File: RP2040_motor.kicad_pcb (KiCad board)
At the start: 4 copper layers, 85.5 x 54 mm, 162 parts, among them J1 USB_C_Receptacle_USB2.0, J2 Conn_01x05, J3 Conn_01x06, J4 Conn_01x04, J5 Conn_01x04, J6 Conn_01x03, SW1 SW_MEC_5G, U1 EG2131, U10 EG2131, U11 RP2040, U2 EG2131, U3 LM358, U4 EG2131, U5 EG2131, U6 XL7045, U7 NCP1117-3.3_SOT223, U8 EG2131, U9 W25Q128JVS, Y1 Crystal_GND24

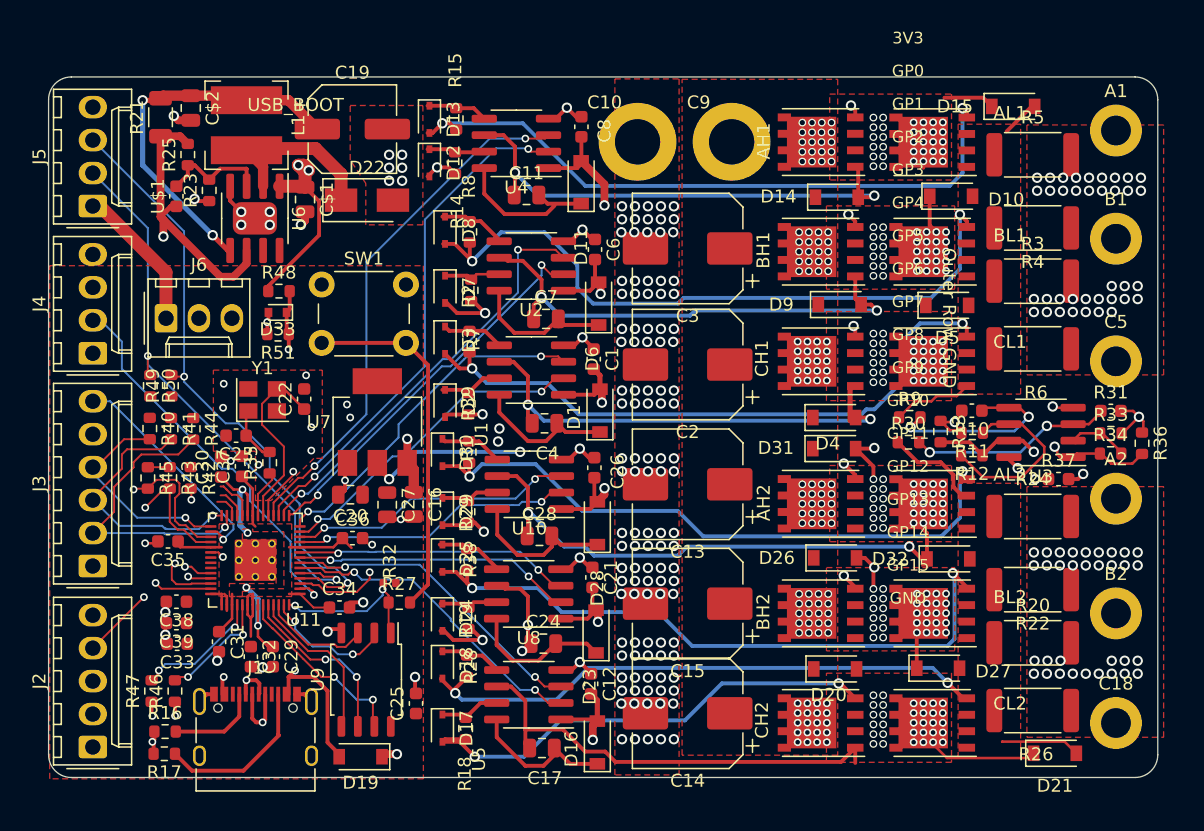
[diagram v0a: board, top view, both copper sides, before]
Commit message: Update files for price quote. DO NOT ORDER THESE BOARDS FROM THIS COMMIT!
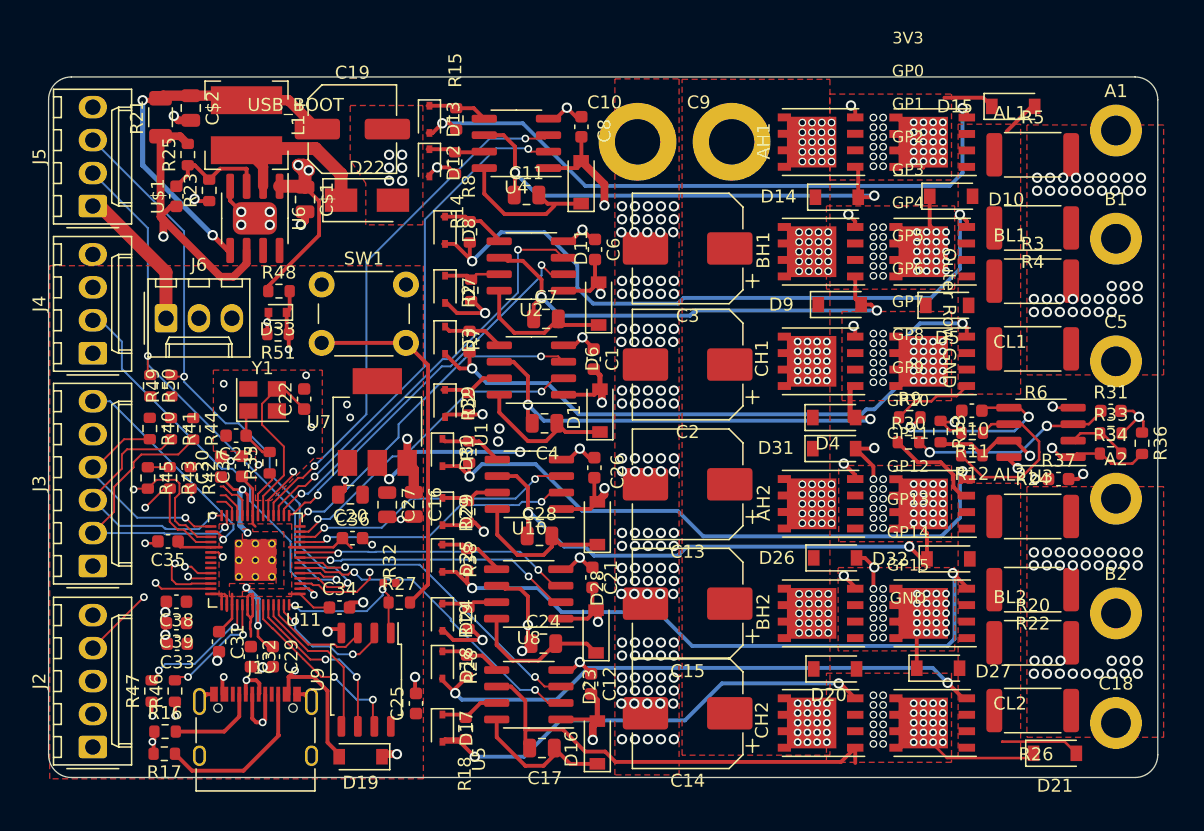
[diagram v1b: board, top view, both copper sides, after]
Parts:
- R51: value 5k -> 5.1k

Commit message: In progress independent phase current measurement.
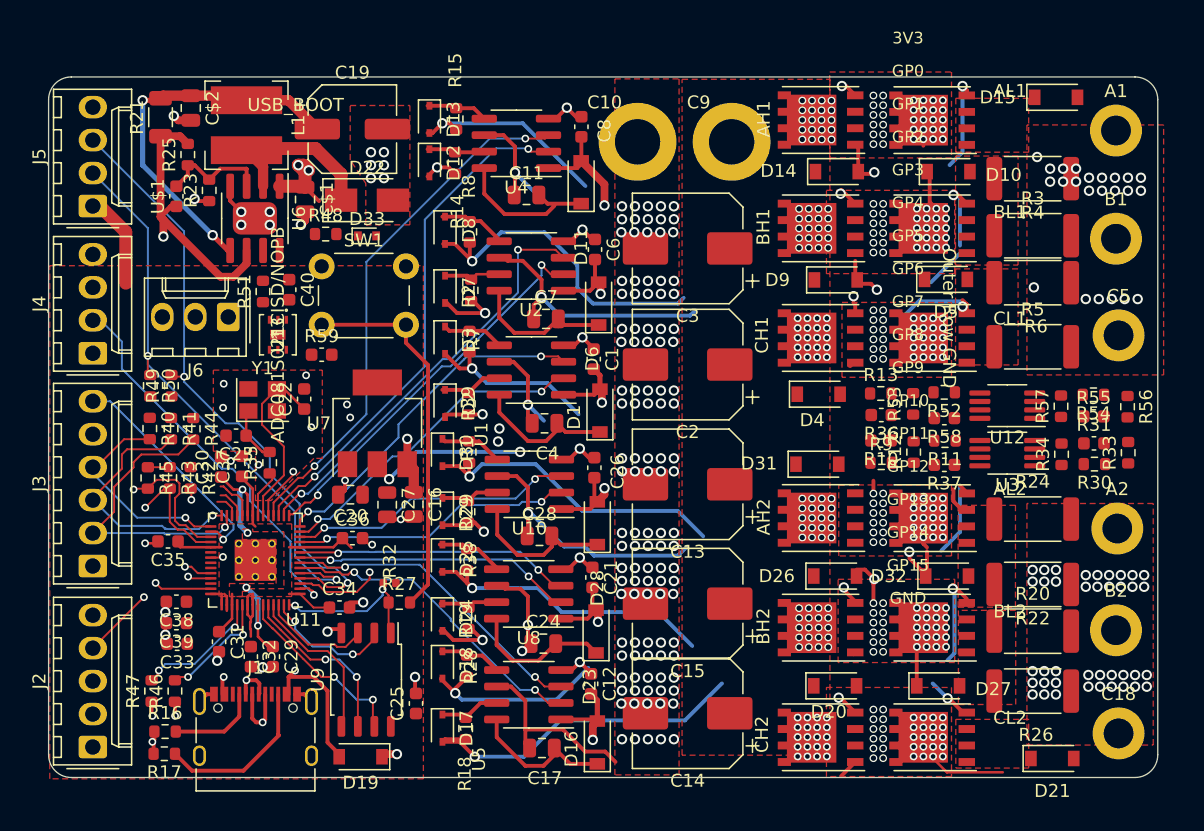
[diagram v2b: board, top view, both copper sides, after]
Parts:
- added C40: 1u, Capacitor_SMD:C_0603_1608Metric, F.Cu at (92.9, 84.4)
- added R52: 4.64k, Resistor_SMD:R_0603_1608Metric, F.Cu at (143.4, 92.3)
- added R53: 133k, Resistor_SMD:R_0603_1608Metric, F.Cu at (141.0, 93.2)
- added R54: 499R, Resistor_SMD:R_0603_1608Metric, F.Cu at (154.9, 92.5)
- added R55: 0.1uF, Capacitor_SMD:C_0603_1608Metric, F.Cu at (154.9, 94.2)
- added R56: 4.64k, Resistor_SMD:R_0603_1608Metric, F.Cu at (157.5, 93.4)
- added R57: 133k, Resistor_SMD:R_0603_1608Metric, F.Cu at (152.4, 93.4)
- added R58: 0.1uF, Capacitor_SMD:C_0603_1608Metric, F.Cu at (143.4, 94.3)
- added R59: 0.1uF, Capacitor_SMD:C_0603_1608Metric, F.Cu at (95.4, 89.4)
- added U12: LM358, Package_SO:MSOP-8_3x3mm_P0.65mm, F.Cu at (148.2, 93.3)
- added U13: ADC081S021CISD/NOPB, ADC081S021:ADC081S021CISD&slash_NOPB, F.Cu at (92.0, 87.9)
- R11, R33: value 6.04k -> 4.64k
- R12, R34: value 88.7K -> 133k
- R13: value DNS -> 499R
- R20, R22, R24, R26, R3, R4, R5, R6: value 8mΩ -> 4mΩ
- R30, R9: value 1.1k -> 499R
- R36: value DNS -> 0.1uF; footprint Resistor_SMD:R_0603_1608Metric -> Capacitor_SMD:C_0603_1608Metric
- U3: footprint Package_SO:SOIC-8_3.9x4.9mm_P1.27mm -> Package_SO:MSOP-8_3x3mm_P0.65mm
- moved R36 20.2 mm to (138.5, 94.1), turned to 180 degrees
- moved R5 14.8 mm to (150.2, 88.8)
- moved R30 14.4 mm to (155.0, 97.8), turned to 180 degrees
- moved D33 9.08 mm to (98.9, 80.2), turned to 0 degrees
- moved R37 8.87 mm to (143.4, 97.9), turned to 180 degrees
- moved R10 7.37 mm to (138.5, 96.0)
- moved R48 5.69 mm to (95.7, 80.1)
- moved R13 5.46 mm to (138.5, 92.4), turned to 0 degrees
- moved R6 5.10 mm to (150.2, 83.9)
- moved J6 4.80 mm to (88.2, 86.5), turned to 180 degrees
- moved R12 4.49 mm to (141.0, 96.9), turned to 90 degrees
- moved R9 4.13 mm to (138.5, 97.7)
- moved R4 3.80 mm to (150.2, 75.8)
- moved R34 3.78 mm to (152.4, 97.1), turned to 90 degrees
- moved R3 3.50 mm to (150.2, 80.2)
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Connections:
- AL1 pad 1: VSENSE2 -> GND
- AL2 pad 1: VSENSE1 -> VSENSE1A
- BL1 pad 1: VSENSE2 -> VSENSE2B
- BL2 pad 1: VSENSE1 -> VSENSE1B
- CL1 pad 1: VSENSE2 -> VSENSE2C
- CL2 pad 1: VSENSE1 -> GND
- D10 pad 2: VSENSE2 -> VSENSE2B
- D15 pad 2: VSENSE2 -> GND
- D21 pad 2: VSENSE1 -> GND
- D27 pad 2: VSENSE1 -> VSENSE1B
- D32 pad 2: VSENSE1 -> VSENSE1A
- D33 pad 1: A3 -> Net-(U13-Pad3)
- D5 pad 2: VSENSE2 -> VSENSE2C
- J6 pad 1: +3V3 -> /RUN
- J6 pad 2: A4 -> /SWCLK
- J6 pad 3: GND -> /SWD
- R12 pad 1: A2 -> A4
- R12 pad 2: Net-(R11-Pad1) -> Net-(R10-Pad1)
- R13 pad 1: GND -> VSENSE2B
- R13 pad 2: A2 -> Net-(R13-Pad2)
- R20 pad 2: VSENSE1 -> VSENSE1B
- R22 pad 2: VSENSE1 -> VSENSE1A
- R24 pad 2: VSENSE1 -> VSENSE1A
- R26 pad 2: VSENSE1 -> VSENSE1B
- R3 pad 2: VSENSE2 -> VSENSE2B
- R30 pad 1: VSENSE1 -> VSENSE1A
- R34 pad 1: A1 -> A3
- R34 pad 2: Net-(R33-Pad1) -> Net-(R30-Pad2)
- R36 pad 1: GND -> Net-(R13-Pad2)
- R36 pad 2: A1 -> GND
- R4 pad 2: VSENSE2 -> VSENSE2B
- R48 pad 2: A3 -> Net-(U13-Pad3)
- R5 pad 2: VSENSE2 -> VSENSE2C
- R51 pad 1: A3 -> Net-(U13-Pad3)
- R6 pad 2: VSENSE2 -> VSENSE2C
- R9 pad 1: VSENSE2 -> VSENSE1B
- U11 pad 34: ENCC -> ADC_CLK
- U11 pad 35: /GPIO23 -> ENCC
- U11 pad 36: /GPIO24 -> ADC_DATA
- U11 pad 37: /GPIO25 -> ADC_CS
- U3 pad 1: A1 -> A3
- U3 pad 7: A2 -> A4
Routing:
- net A1: track 89.8 -> 37.4 mm, vias 4 -> 3
- net A2: track 86.8 -> 38.7 mm, vias 4 -> 3
- net +3V3: track 95.7 -> 55.3 mm, vias 4 -> 2
- net Net-(CH1-Pad2): track 38.8 -> 4.06 mm
- net A3: track 30.0 -> 0.00 mm, vias 2 -> 0
- net M2A: track 43.2 -> 13.3 mm
- net M2C: track 37.2 -> 8.33 mm, vias 34 -> 33
- net Net-(AL1-Pad2): track 51.1 -> 23.0 mm
- net Net-(CL2-Pad2): track 44.8 -> 18.3 mm
- net Net-(CL1-Pad2): track 49.3 -> 23.0 mm
- net Net-(BH1-Pad2): track 39.5 -> 16.1 mm
- net Net-(AH1-Pad2): track 42.6 -> 21.0 mm
- net M1C: track 45.0 -> 23.9 mm
- net M1A: track 46.7 -> 26.2 mm, vias 35 -> 34
- net Net-(BL2-Pad2): track 50.5 -> 30.8 mm
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- added copper zone on F.Cu, net VSENSE1A
- added copper zone on F.Cu, net VSENSE1B
- added copper zone on F.Cu, net VSENSE2B
- added copper zone on F.Cu, net VSENSE2C
- removed copper zone on F.Cu, net VSENSE1
- removed copper zone on F.Cu, net VSENSE2

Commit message: Break out to two page schematic. Update images and schematic PDF
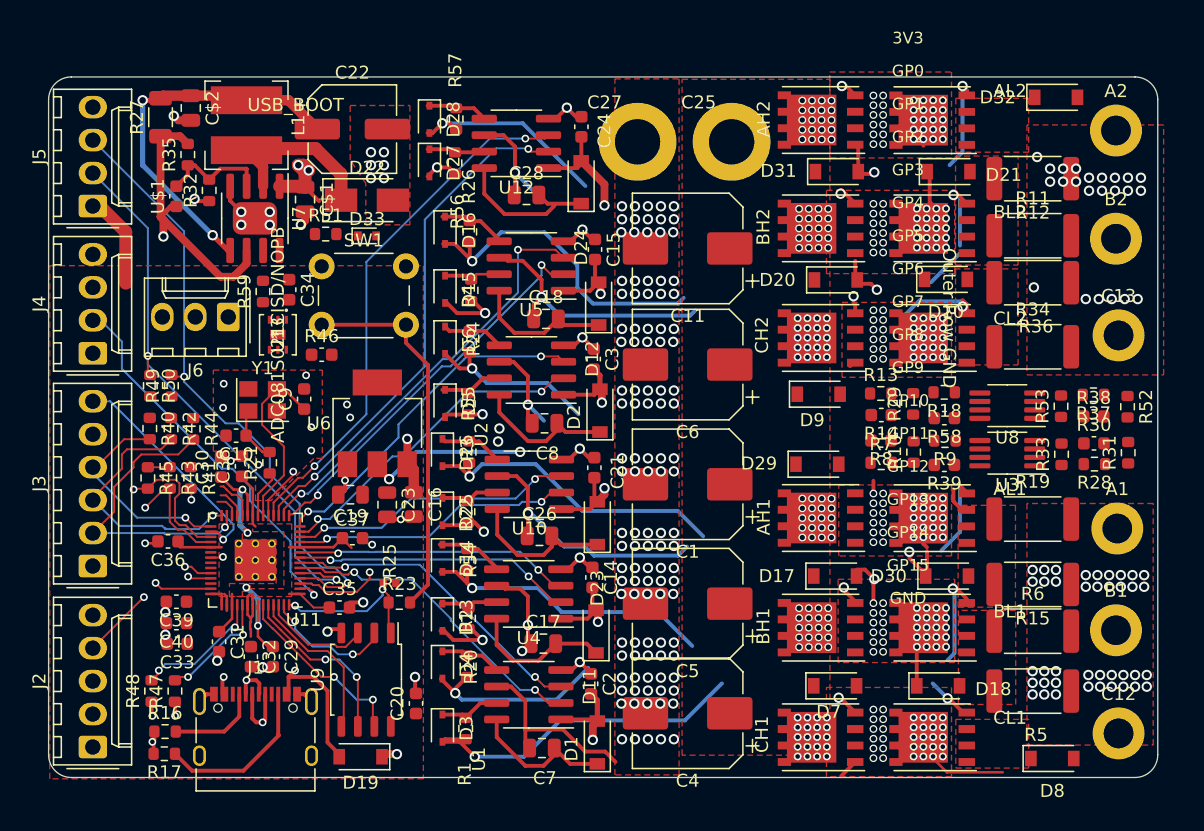
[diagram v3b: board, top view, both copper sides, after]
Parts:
- renumbered A2 to A1, A1 to A2, AH2 to AH1, AH1 to AH2, AL2 to AL1, AL1 to AL2, B2 to B1, B1 to B2, BH2 to BH1, BH1 to BH2, BL2 to BL1, BL1 to BL2, C13 to C1, C23 to C10, C3 to C11, C18 to C12, C5 to C13, C21 to C14, C6 to C15, C24 to C17, C7 to C18, C20 to C19, C12 to C2, C25 to C20, C26 to C21, C19 to C22, C27 to C23, C8 to C24, C9 to C25, C28 to C26, C10 to C27, C11 to C28, C1 to C3, C40 to C34, C34 to C35, C35 to C36, C36 to C37, C37 to C38, C38 to C39, C14 to C4, C39 to C40, C15 to C5, C2 to C6, C17 to C7, C4 to C8, C22 to C9, CH2 to CH1, CH1 to CH2, CL2 to CL1, CL1 to CL2, D16 to D1, D5 to D10, D23 to D11, D6 to D12, D24 to D13, D25 to D14, D7 to D15, D8 to D16, D26 to D17, D27 to D18, D1 to D2, D9 to D20, D10 to D21, D28 to D23, D11 to D24, D29 to D25, D30 to D26, D12 to D27, D13 to D28, D31 to D29, D17 to D3, D32 to D30, D14 to D31, D15 to D32, D18 to D4, D2 to D5, D3 to D6, D20 to D7, D21 to D8, D4 to D9, R18 to R1, R12 to R10, R3 to R11, R4 to R12, R36 to R14, R22 to R15, R52 to R18, R24 to R19, R19 to R2, R28 to R20, R35 to R21, R29 to R22, R27 to R23, R7 to R24, R32 to R25, R8 to R26, R21 to R27, R30 to R28, R53 to R29, R1 to R3, R31 to R30, R33 to R31, R23 to R32, R34 to R33, R5 to R34, R25 to R35, R6 to R36, R54 to R37, R55 to R38, R37 to R39, R2 to R4, R42 to R41, R41 to R42, R59 to R46, R46 to R47, R47 to R48, R26 to R5, R48 to R51, R56 to R52, R57 to R53, R38 to R54, R39 to R55, R14 to R56, R15 to R57, R51 to R59, R20 to R6, R9 to R7, R10 to R8, R11 to R9, U5 to U1, U4 to U12, U1 to U2, U8 to U4, U2 to U5, U7 to U6, U6 to U7, U12 to U8
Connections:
- net /QSPI_SCLK renamed /power_and_cpu/QSPI_SCLK
- net /QSPI_SD0 renamed /power_and_cpu/QSPI_SD0
- net /QSPI_SD1 renamed /power_and_cpu/QSPI_SD1
- net /QSPI_SD2 renamed /power_and_cpu/QSPI_SD2
- net /QSPI_SD3 renamed /power_and_cpu/QSPI_SD3
- net /QSPI_SS renamed /power_and_cpu/QSPI_SS
- net /RUN renamed /power_and_cpu/RUN
- net /SWCLK renamed /power_and_cpu/SWCLK
- net /SWD renamed /power_and_cpu/SWD
- net /USB_D+ renamed /power_and_cpu/USB_D+
- net /USB_D- renamed /power_and_cpu/USB_D-
- net /XIN renamed /power_and_cpu/XIN
- net /XOUT renamed /power_and_cpu/XOUT
- net /~{USB_BOOT} renamed /power_and_cpu/~{USB_BOOT}
- U1 pad 2: /GPIO4 -> /gate_drive/GPIO4
- U1 pad 3: /GPIO5 -> /gate_drive/GPIO5
- U10 pad 2: /GPIO8 -> /gate_drive/GPIO8
- U10 pad 3: /GPIO9 -> /gate_drive/GPIO9
- U11 pad 11: /GPIO8 -> /power_and_cpu/GPIO8
- U11 pad 12: /GPIO9 -> /power_and_cpu/GPIO9
- U11 pad 13: /GPIO10 -> /power_and_cpu/GPIO10
- U11 pad 14: /GPIO11 -> /power_and_cpu/GPIO11
- U11 pad 15: /GPIO12 -> /power_and_cpu/GPIO12
- U11 pad 16: /GPIO13 -> /power_and_cpu/GPIO13
- U11 pad 17: /GPIO14 -> /power_and_cpu/GPIO14
- U11 pad 18: /GPIO15 -> /power_and_cpu/GPIO15
- U11 pad 6: /GPIO4 -> /power_and_cpu/GPIO4
- U11 pad 7: /GPIO5 -> /power_and_cpu/GPIO5
- U11 pad 8: /GPIO6 -> /power_and_cpu/GPIO6
- U11 pad 9: /GPIO7 -> /power_and_cpu/GPIO7
- U12 pad 2: /GPIO14 -> /gate_drive/GPIO14
- U12 pad 3: /GPIO15 -> /gate_drive/GPIO15
- U2 pad 2: /GPIO10 -> /gate_drive/GPIO10
- U2 pad 3: /GPIO11 -> /gate_drive/GPIO11
- U4 pad 2: /GPIO6 -> /gate_drive/GPIO6
- U4 pad 3: /GPIO7 -> /gate_drive/GPIO7
- U5 pad 2: /GPIO12 -> /gate_drive/GPIO12
- U5 pad 3: /GPIO13 -> /gate_drive/GPIO13
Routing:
- net /power_and_cpu/GPIO15: track 0.00 -> 40.8 mm, vias 0 -> 2
- net /GPIO15: track 40.8 -> 0.00 mm, vias 2 -> 0
- net /gate_drive/GPIO14: track 0.00 -> 39.7 mm, vias 0 -> 2
- net /GPIO14: track 39.7 -> 0.00 mm, vias 2 -> 0
- net /power_and_cpu/GPIO13: track 0.00 -> 32.5 mm, vias 0 -> 2
- net /GPIO13: track 32.5 -> 0.00 mm, vias 2 -> 0
- net /power_and_cpu/GPIO12: track 0.00 -> 30.1 mm, vias 0 -> 2
- net /GPIO12: track 30.1 -> 0.00 mm, vias 2 -> 0
- net /gate_drive/GPIO11: track 0.00 -> 26.8 mm, vias 0 -> 2
- net /GPIO11: track 26.8 -> 0.00 mm, vias 2 -> 0
- net /power_and_cpu/GPIO10: track 0.00 -> 25.4 mm, vias 0 -> 2
- net /GPIO10: track 25.4 -> 0.00 mm, vias 2 -> 0
- net /power_and_cpu/GPIO4: track 0.00 -> 24.7 mm, vias 0 -> 2
- net /GPIO4: track 24.7 -> 0.00 mm, vias 2 -> 0
- net /gate_drive/GPIO5: track 0.00 -> 24.2 mm, vias 0 -> 2
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
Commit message: Updated design rules and fixed routing to eliminate all copper DRC errors.
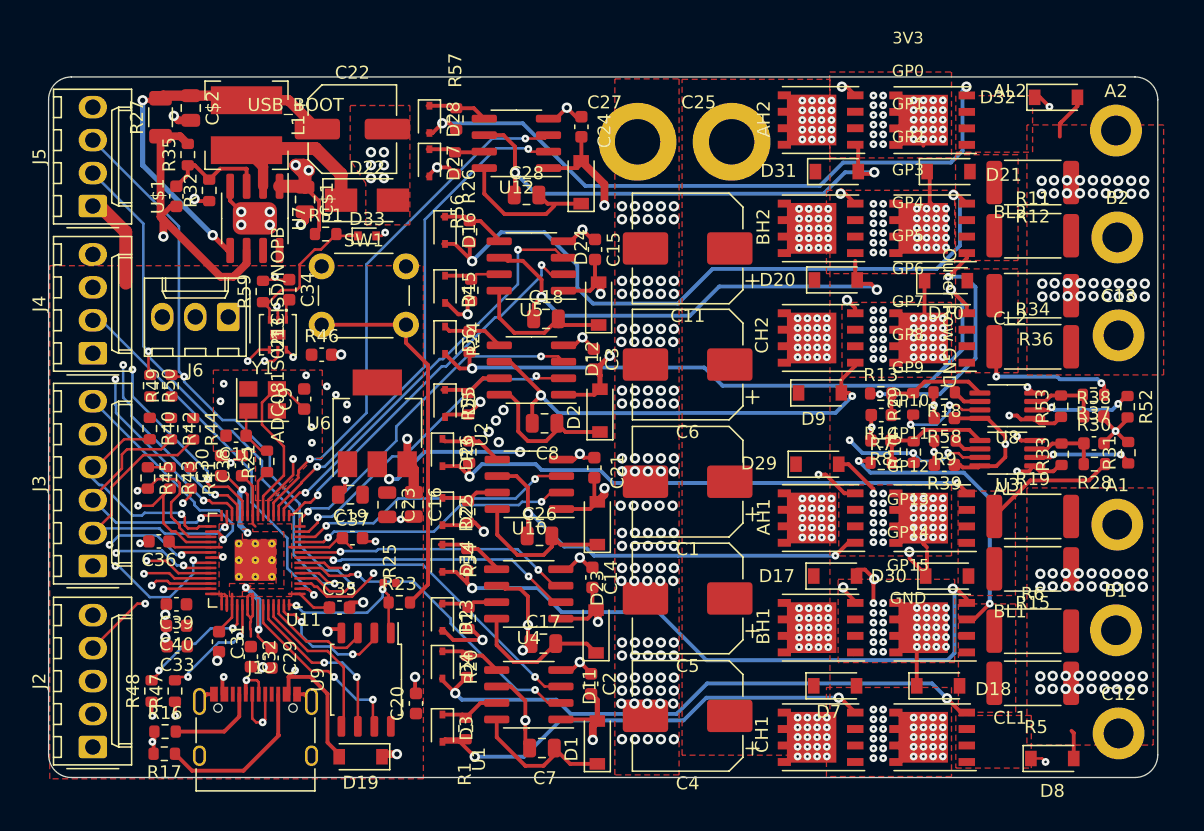
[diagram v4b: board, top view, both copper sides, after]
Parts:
- moved R15 1.20 mm to (150.2, 105.9)
- moved R36 1.00 mm to (150.2, 84.9)
- moved C36 0.70 mm to (82.8, 103.8)
- moved R5 0.60 mm to (150.2, 114.7)
- moved C5 0.40 mm to (123.6, 108.2)
- moved A1 0.30 mm to (156.7, 102.5)
- moved R12 0.30 mm to (150.2, 76.1)
- moved R21 0.22 mm to (91.2, 97.6)
- moved C1 0.20 mm to (123.6, 99.2)
- moved C33 0.20 mm to (84.3, 111.9)
- moved C39 0.20 mm to (84.2, 108.7)
- moved C4 0.20 mm to (123.6, 117.2)
- moved C40 0.20 mm to (84.2, 110.3)
- moved R19 0.20 mm to (150.2, 101.9)
- moved D9 0.14 mm to (133.8, 92.4)
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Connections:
- U1 pad 2: /gate_drive/GPIO4 -> GPIO4
- U1 pad 3: /gate_drive/GPIO5 -> GPIO5
- U10 pad 2: /gate_drive/GPIO8 -> GPIO8
- U10 pad 3: /gate_drive/GPIO9 -> GPIO9
- U11 pad 11: /power_and_cpu/GPIO8 -> GPIO8
- U11 pad 12: /power_and_cpu/GPIO9 -> GPIO9
- U11 pad 13: /power_and_cpu/GPIO10 -> GPIO10
- U11 pad 14: /power_and_cpu/GPIO11 -> GPIO11
- U11 pad 15: /power_and_cpu/GPIO12 -> GPIO12
- U11 pad 16: /power_and_cpu/GPIO13 -> GPIO13
- U11 pad 17: /power_and_cpu/GPIO14 -> GPIO14
- U11 pad 18: /power_and_cpu/GPIO15 -> GPIO15
- U11 pad 6: /power_and_cpu/GPIO4 -> GPIO4
- U11 pad 7: /power_and_cpu/GPIO5 -> GPIO5
- U11 pad 8: /power_and_cpu/GPIO6 -> GPIO6
- U11 pad 9: /power_and_cpu/GPIO7 -> GPIO7
- U12 pad 2: /gate_drive/GPIO14 -> GPIO14
- U12 pad 3: /gate_drive/GPIO15 -> GPIO15
- U2 pad 2: /gate_drive/GPIO10 -> GPIO10
- U2 pad 3: /gate_drive/GPIO11 -> GPIO11
- U4 pad 2: /gate_drive/GPIO6 -> GPIO6
- U4 pad 3: /gate_drive/GPIO7 -> GPIO7
- U5 pad 2: /gate_drive/GPIO12 -> GPIO12
- U5 pad 3: /gate_drive/GPIO13 -> GPIO13
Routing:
- net A3: track 0.00 -> 91.1 mm, vias 0 -> 4
- net A4: track 17.9 -> 78.8 mm, vias 1 -> 6
- net A1: track 37.4 -> 87.0 mm, vias 3 -> 4
- net ADC_DATA: track 0.00 -> 48.4 mm, vias 0 -> 3
- net +3V3: track 55.3 -> 99.1 mm, vias 2 -> 3
- net A2: track 38.7 -> 82.0 mm, vias 3 -> 5
- net GPIO15: track 0.00 -> 41.0 mm, vias 0 -> 2
- net /power_and_cpu/GPIO15: track 40.8 -> 0.00 mm, vias 2 -> 0
- net GPIO14: track 0.00 -> 39.7 mm, vias 0 -> 2
- net /gate_drive/GPIO14: track 39.7 -> 0.00 mm, vias 2 -> 0
- net Net-(CH2-Pad2): track 4.06 -> 38.5 mm
- net /power_and_cpu/GPIO13: track 32.5 -> 0.00 mm, vias 2 -> 0
- net GPIO13: track 0.00 -> 32.2 mm, vias 0 -> 2
- net ADC_CS: track 0.00 -> 32.0 mm, vias 0 -> 3
- net ADC_CLK: track 0.00 -> 30.4 mm, vias 0 -> 3
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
